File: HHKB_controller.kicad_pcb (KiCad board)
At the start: 2 copper layers, 141.5 x 36 mm, 82 parts, among them CN1 CONN_15, CN2 CONN_13, J1 USB_MINI_MICRO_B, P15 ICSP, P16 CONN_2, P21 CONN_1, P22 CONN_1, P23 CONN_1, P24 CONN_1, P25 CONN_1, P26 CONN_1, P27 CONN_1, P28 CONN_1, P29 CONN_1, Q1 MOSFET_N, Q2 MOSFET_N, SW1 SW_PUSH, SW2 SPST, U1 ATMEGA32U4, U2 TAR5SB33, U3 HT7750A, U4 LTC4054, X1 16MHz

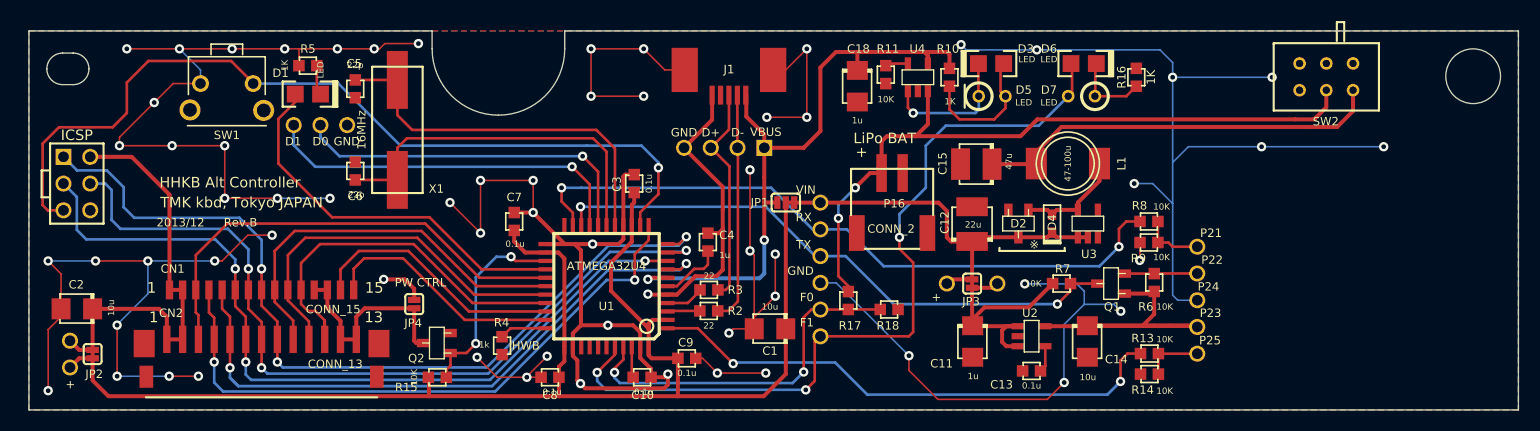
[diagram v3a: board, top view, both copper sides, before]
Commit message: Design initial Rev.B PCB
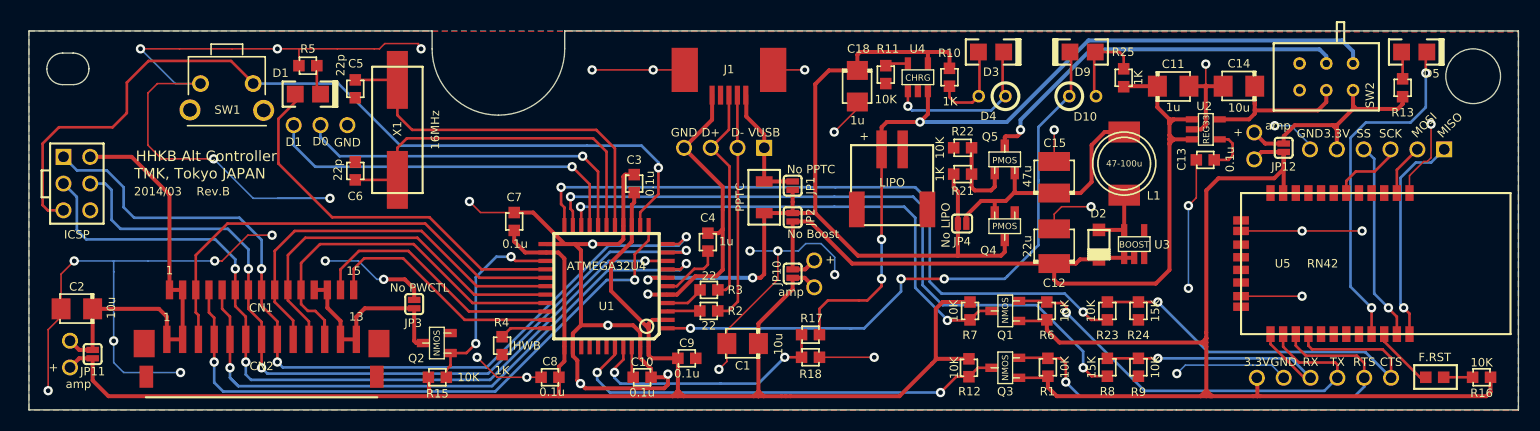
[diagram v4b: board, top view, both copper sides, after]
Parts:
- removed D6: LED, LED_2012_HSOL
- removed D7: LED, LED_TH
- removed F0, F1, P21, P22, P23, P24, P25, P26, P27, P28, P29, RX, TX, VIN: CONN_1, PIN_1
- removed the GND at (152.1, 104.7)
- removed the GND at (100.3, 87.7)
- removed P15: ICSP, AVR_ICSP_3x2
- removed P16: CONN_2, JST_PH2_SMT
- removed R14: 10K, R_1608
- removed VBUS: CONN_1, PIN_1_SQUARE
- added D10: LED, LED_TH, F.Cu at (177.0, 87.0)
- added D9: LED, LED_2012_HSOL, F.Cu at (177.0, 82.8)
- added GND: CONN_1, PIN_1, F.Cu at (107.2, 89.8)
- added JP10: JUMPER, SOLDER_JUMPER_2, F.Cu at (149.4, 103.8)
- added JP11: JUMPER, SOLDER_JUMPER_2, F.Cu at (83.0, 111.5)
- added JP12: JUMPER, SOLDER_JUMPER_2, F.Cu at (196.1, 91.9)
- added P10: CONN_1, PIN_1, F.Cu at (80.8, 110.2)
- added P100: CONN_2, JST_PH2_SMT, F.Cu at (157.9, 92.0)
- added P11: CONN_1, PIN_1, F.Cu at (151.5, 102.6)
- added P110: CONN_1, PIN_1, F.Cu at (193.6, 113.8)
- added P111: CONN_1, PIN_1, F.Cu at (198.7, 113.8)
- added P112: CONN_1, PIN_1, F.Cu at (201.2, 113.8)
- added P113: CONN_1, PIN_1, F.Cu at (196.1, 113.8)
- added P114: CONN_1, PIN_1, F.Cu at (206.3, 113.8)
- added P115: CONN_1, PIN_1, F.Cu at (203.8, 113.8)
- added P12: CONN_1, PIN_1, F.Cu at (151.5, 105.2)
- added P120: CONN_1, PIN_1_SQUARE, F.Cu at (211.3, 92.0)
- added P121: CONN_1, PIN_1, F.Cu at (208.8, 92.0)
- added P122: CONN_1, PIN_1, F.Cu at (206.2, 92.0)
- added P123: CONN_1, PIN_1, F.Cu at (203.7, 92.0)
- added P124: CONN_1, PIN_1, F.Cu at (201.2, 92.0)
- added P125: CONN_1, PIN_1, F.Cu at (198.6, 92.0)
- added P130: CONN_1, PIN_1, F.Cu at (193.3, 90.5)
- added P131: CONN_1, PIN_1, F.Cu at (193.3, 93.0)
- added P8: CONN_3X2, AVR_ICSP_3x2, F.Cu at (81.5, 95.3)
- added P9: CONN_1, PIN_1, F.Cu at (80.8, 112.8)
- added PPTC1: PPTC, PPTC_nano, F.Cu at (146.8, 96.6)
- added Q3: NMOS, MOS_FET_SOT23-3_HSOL, F.Cu at (169.7, 112.8)
- added Q4: PMOS, MOS_FET_SOT23-3_HSOL, F.Cu at (169.6, 99.3)
- added Q5: PMOS, MOS_FET_SOT23-3_HSOL, F.Cu at (169.6, 93.0)
- added R1: 10K, R_1608, F.Cu at (173.7, 112.8)
- added R12: 10K, R_1608, F.Cu at (166.2, 112.8)
- added R19: 0, R_1608_NOGUIDE, F.Cu at (210.4, 113.7)
- added R21: 1K, R_1608, F.Cu at (165.6, 94.4)
- added R22: 10K, R_1608, F.Cu at (165.6, 91.9)
- added R23: 10K, R_1608, F.Cu at (179.3, 107.4)
- added R24: 15K, R_1608, F.Cu at (182.3, 107.4)
- added R25: 1K, R_1608, F.Cu at (180.9, 85.2)
- added U5: RN42, RN42, F.Cu at (208.1, 96.2)
- added VUSB: CONN_1, PIN_1_SQUARE, F.Cu at (146.8, 91.9)
- D2: value MA721 -> Schottky; footprint SOT23-3_HSOL -> D_SOD123
- D4: value RB521 -> LED; footprint D_SC79 -> LED_TH
- D5: footprint LED_TH -> LED_2012_HSOL
- JP1: value JUMPER3 -> JUMPER; footprint SOLDER_JUMPER_3 -> SOLDER_JUMPER_2
- Q1, Q2: value MOSFET_N -> NMOS
- R13: value 10K -> 470
- R16: value 1K -> 10K
- R4: value 1k -> 1K
- R9: value 10K -> 15K
- SW2: value SPST -> SW_DPDT
- U2: value TAR5SB33 -> REG33
- U3: value HT7750A -> BOOST
- U4: value LTC4054 -> CHRG
- moved JP2 67.8 mm to (149.4, 98.5), turned to 270 degrees
- moved JP3 53.0 mm to (113.5, 106.8), turned to 270 degrees
- moved JP4 52.6 mm to (165.6, 99.1), turned to 0 degrees
- moved R16 43.5 mm to (214.9, 113.7), turned to 180 degrees
- moved D5 40.3 mm to (208.5, 82.8), turned to 0 degrees
- moved R13 34.9 mm to (207.4, 86.2), turned to 90 degrees
- moved C11 30.8 mm to (185.6, 86.0), turned to 0 degrees
- moved C14 28.2 mm to (191.8, 86.0), turned to 180 degrees
- moved C13 26.0 mm to (188.7, 93.0)
- moved U2 25.7 mm to (188.7, 90.2)
- moved R8 14.4 mm to (179.3, 112.8), turned to 90 degrees
- moved D4 13.4 mm to (168.4, 87.0), turned to 0 degrees
- moved R9 11.9 mm to (182.3, 112.8), turned to 270 degrees
- moved R6 10.6 mm to (173.6, 107.4)
- moved Q1 10.4 mm to (169.7, 107.4)
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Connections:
- net BT_LIPO renamed LIPO_SENSE
- C1 pad 1: VIN -> 5V_BOOST
- C11 pad 1: VIN -> 5V_BOOST
- C12 pad 1: VIN -> 5V_BOOST
- C14 pad 1: +3.3V -> /bluetooth/3.3V_OUT
- C15 pad 1: /bluetooth/VBAT -> /bluetooth/PSEL
- C18 pad 1: VBUS -> VUSB
- C2 pad 1: VIN -> 5V_BOOST
- C3 pad 1: VIN -> 5V_BOOST
- C7 pad 1: VIN -> 5V_BOOST
- C8 pad 1: VIN -> 5V_BOOST
- C9 pad 1: VIN -> 5V_BOOST
- CN1 pad 1: VIN -> 5V_BOOST
- CN1 pad 2: VIN -> 5V_BOOST
- CN2 pad 1: VIN -> 5V_BOOST
- CN2 pad 2: VIN -> 5V_BOOST
- D2 pad 1: N-0000051 -> N-0000064
- D2 pad 2: N-0000075 -> 5V_BOOST
- D3 pad 1: N-0000069 -> N-0000067
- D3 pad 2: N-0000046 -> N-0000049
- D4 pad 1: N-0000051 -> N-0000067
- D4 pad 2: VIN -> N-0000049
- D5 pad 1: N-0000069 -> N-0000046
- D5 pad 2: N-0000046 -> /bluetooth/LED_STS
- J1 pad 1: VBUS -> /VUSB_RAW
- JP1 pad 1: VBUS -> /VUSB_RAW
- JP1 pad 2: VIN -> VUSB
- JP2 pad 1: VIN -> VUSB
- JP2 pad 2: VIN -> 5V_BOOST
- JP3 pad 1: VIN -> GND
- JP3 pad 2: VIN -> /HHKB_GND
- JP4 pad 1: GND -> VUSB
- JP4 pad 2: /HHKB_GND -> /bluetooth/PSEL
- L1 pad 1: N-0000051 -> N-0000064
- L1 pad 2: /bluetooth/VBAT -> /bluetooth/PSEL
- R10 pad 1: N-0000069 -> N-0000067
- R10 pad 2: VBUS -> VUSB
- R13 pad 1: BT_DTR -> +3.3V
- R13 pad 2: /bluetooth/DTR_33 -> N-0000046
- R15 pad 1: VIN -> 5V_BOOST
- R16 pad 1: N-0000045 -> +3.3V
- R16 pad 2: GND -> N-0000043
- R17 pad 1: N-0000047 -> /bluetooth/LIPO_RAW
- R7 pad 1: VIN -> 5V_BOOST
- SW2 pad 1: N-0000047 -> /bluetooth/LIPO_SW
- SW2 pad 2: /bluetooth/VBAT -> /bluetooth/LIPO_RAW
- SW2 pad 3: (no net) -> N-0000059
- SW2 pad 4: (no net) -> /bluetooth/3.3V_OUT
- SW2 pad 5: (no net) -> +3.3V
- SW2 pad 6: (no net) -> N-0000060
- U1 pad 1: BT_DTR -> BT_INDICATOR
- U1 pad 14: VIN -> 5V_BOOST
- U1 pad 2: VIN -> 5V_BOOST
- U1 pad 22: /PD5 -> BT_CTS
- U1 pad 24: VIN -> 5V_BOOST
- U1 pad 34: VIN -> 5V_BOOST
- U1 pad 40: BT_INDICATOR -> BT_RTS
- U1 pad 44: VIN -> 5V_BOOST
- U1 pad 7: VBUS -> VUSB
- U2 pad 1: VIN -> 5V_BOOST
- U2 pad 3: VIN -> 5V_BOOST
- U2 pad 5: +3.3V -> /bluetooth/3.3V_OUT
- U3 pad 1: VIN -> 5V_BOOST
- U3 pad 2: VIN -> 5V_BOOST
- U3 pad 5: N-0000051 -> N-0000064
- U4 pad 1: N-0000046 -> N-0000049
- U4 pad 3: N-0000047 -> /bluetooth/LIPO_RAW
- U4 pad 4: VBUS -> VUSB
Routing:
- net 5V_BOOST: track 0.00 -> 288.8 mm
- net VIN: track 243.0 -> 0.00 mm
- net +3.3V: track 31.4 -> 130.6 mm
- net GND: track 438.5 -> 346.1 mm, vias 64 -> 41
- net VUSB: track 0.00 -> 84.6 mm, vias 0 -> 2
- net /bluetooth/LIPO_RAW: track 0.00 -> 77.4 mm, vias 0 -> 3
- net N-0000047: track 67.0 -> 0.00 mm, vias 2 -> 0
- net BT_CTS: track 0.00 -> 65.4 mm, vias 0 -> 2
- net VBUS: track 61.4 -> 0.00 mm, vias 2 -> 0
- net BT_DTR: track 50.5 -> 0.00 mm, vias 2 -> 0
- net /bluetooth/RTS_33: track 0.00 -> 46.2 mm, vias 0 -> 1
- net BT_RTS: track 0.00 -> 42.8 mm, vias 0 -> 2
- net /bluetooth/CTS_33: track 0.00 -> 41.3 mm, vias 0 -> 1
- net /bluetooth/VBAT: track 39.0 -> 0.00 mm
- net /bluetooth/LIPO_SW: track 0.00 -> 36.5 mm, vias 0 -> 1
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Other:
- board text added: "2014/03"
- board text added: "3.3V"
- board text added: "CTS"
- board text added: "F.RST"
- board text added: "GND"
- board text added: "LIPO"
- board text added: "MISO"
- board text added: "MOSI"
- board text added: "No Boost"
- board text added: "No LIPO"
- board text added: "No PPTC"
- board text added: "No PWCTL"
- board text added: "RTS"
- board text added: "RX"
- board text added: "SCK"
- board text added: "SS"
- board text added: "TMK, Tokyo JAPAN"
- board text added: "TX"
- board text added: "amp"
- board text removed: "2013/12"
- board text removed: "LiPo BAT"
- board text removed: "PW CTRL"
- board text removed: "TMK kbd, Tokyo JAPAN"
- board text removed: "※"

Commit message: Clean files
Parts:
- moved D5 22.8 mm to (185.7, 82.8), turned to 180 degrees
- moved R13 17.2 mm to (190.6, 82.8), turned to 180 degrees
- moved R25 0.40 mm to (180.7, 85.6)
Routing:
- net GND: track 346.1 -> 448.7 mm, vias 41 -> 50
- net +3.3V: track 130.6 -> 147.6 mm
- net N-0000049: track 15.8 -> 22.2 mm
- net /bluetooth/LED_STS: track 33.1 -> 37.5 mm
- net /bluetooth/LIPO_RAW: track 77.4 -> 80.3 mm
- net /PB4: track 37.9 -> 36.6 mm
- net BT_CTS: track 65.4 -> 66.2 mm
- net /PB5: track 36.3 -> 35.5 mm
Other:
- board text added: "HHKB Alt Controller TMK, Tokyo JAPAN"
- board text added: "LiPo"
- board text added: "No LiPo"
- board text removed: "HHKB Alt Controller"
- board text removed: "LIPO"
- board text removed: "No LIPO"
- board text removed: "TMK, Tokyo JAPAN"

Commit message: Change module for Schottky diode D2
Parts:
- D2: footprint D_SOD123 -> keyboard_parts:D_SOD123
- moved D2 0.23 mm to (178.3, 101.0)

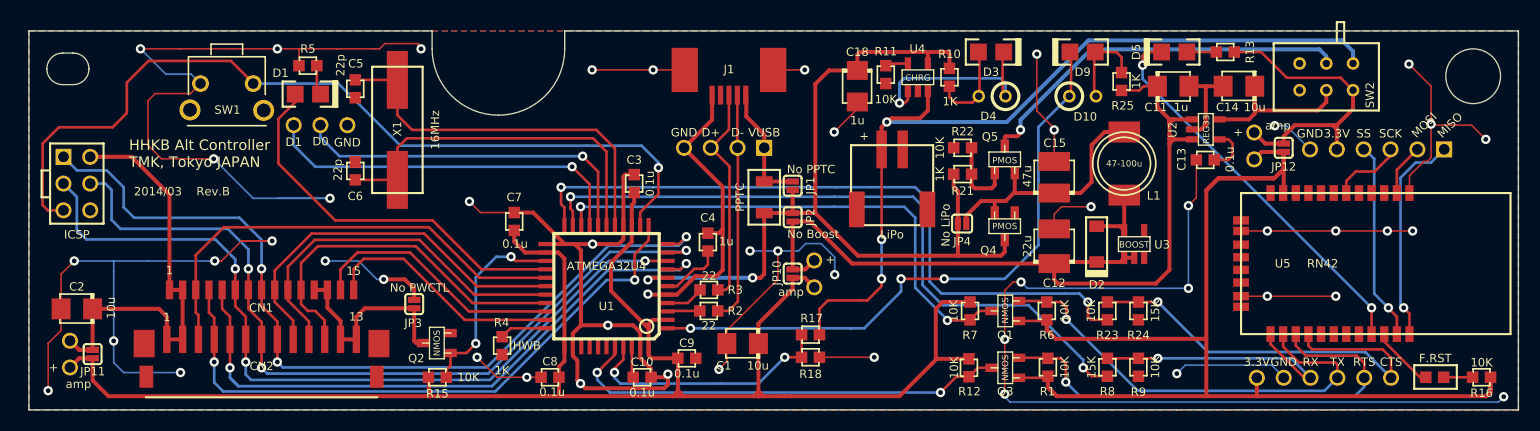
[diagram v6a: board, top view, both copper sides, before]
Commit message: Fix many fixes of rev.B errata
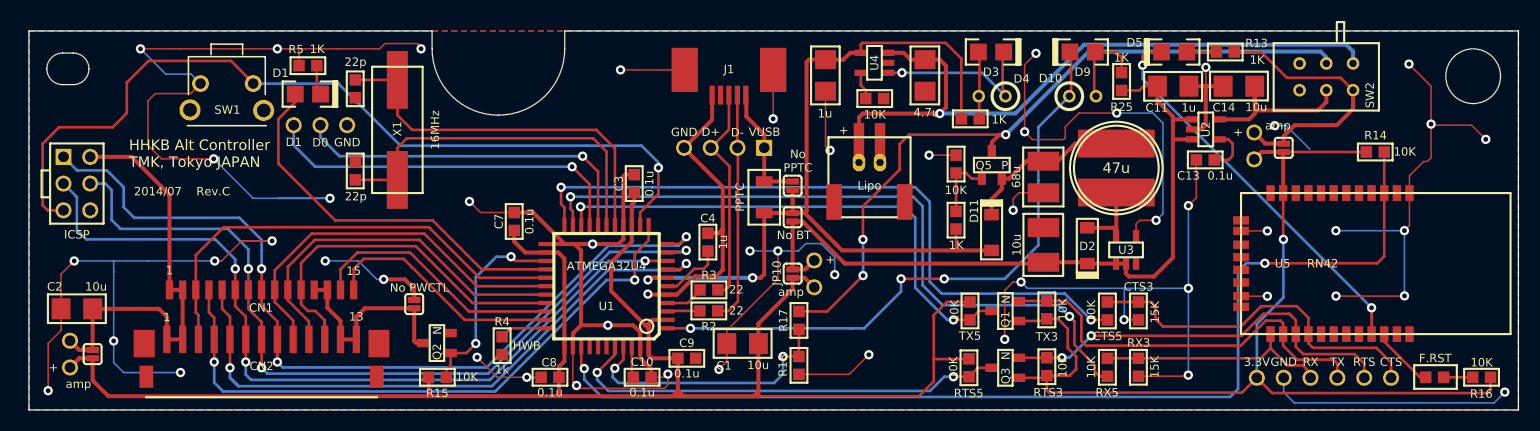
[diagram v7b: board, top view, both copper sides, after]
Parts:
- removed D0, P121, P122, P123, P124, P125: CONN_1, PIN_1
- removed JP4: JUMPER, SOLDER_JUMPER_2
- removed P120: CONN_1, PIN_1_SQUARE
- removed Q4: PMOS, MOS_FET_SOT23-3_HSOL
- added C16: 4.7u, keyboard_parts:C_3216, F.Cu at (162.0, 85.0)
- added D11: Schottky diode, keyboard_parts:D_SOD123, F.Cu at (168.3, 100.0)
- added P6: D0, keyboard_parts:PIN_1, F.Cu at (104.6, 89.8)
- added R14: 10K, keyboard_parts:R_1608, F.Cu at (204.8, 92.3)
- C1, C11, C14, C18, C2: footprint C_3216 -> keyboard_parts:C_3216
- C10, C13, C3, C4, C5, C6, C7, C8, C9: footprint C_1608 -> keyboard_parts:C_1608
- C12: value 22u -> 10u; footprint C_3228 -> keyboard_parts:C_3228
- C15: value 47u -> 68u; footprint C_3225 -> keyboard_parts:C_3225
- D2: value Schottky -> Schottky diode
- J1: value USB_MINI_MICRO_B -> USB_mini_micro_B
- L1: value 47-100u -> 47u; footprint L_6x6MM -> keyboard_parts:L_7x7MM
- P1, P7: renamed from GND; value CONN_1 -> GND
- P100: value CONN_2 -> Lipo; footprint JST_PH2_SMT -> keyboard_parts:JST_PH2_SMT_TH
- P2: renamed from D+; value CONN_1 -> D+
- P3: renamed from D-; value CONN_1 -> D-
- P4: renamed from VUSB; value CONN_1 -> VUSB
- P5: renamed from D1; value CONN_1 -> D1
- Q1, Q2, Q3: value NMOS -> N; footprint MOS_FET_SOT23-3_HSOL -> keyboard_parts:MOS_FET_SOT23-3_HSOL
- Q5: value PMOS -> P; footprint MOS_FET_SOT23-3_HSOL -> keyboard_parts:MOS_FET_SOT23-3_HSOL
- R1, R10, R11, R12, R15, R16, R17, R18, R2, R21, R22, R23, R24, R25, R3, R5, R6, R7, R8, R9: footprint R_1608 -> keyboard_parts:R_1608
- R13: value 470 -> 1K; footprint R_1608 -> keyboard_parts:R_1608
- R4: value 1K -> 1k; footprint R_1608 -> keyboard_parts:R_1608
- U2: value REG33 -> TAR5SB33; footprint SOT23-5_HSOL -> keyboard_parts:SOT23-5_HSOL
- U3: value BOOST -> NCP1402; footprint SOT23-5_HSOL -> keyboard_parts:SOT23-5_HSOL
- U4: value CHRG -> MCP73831; footprint SOT23-5_HSOL -> keyboard_parts:SOT23-5_HSOL
- moved R21 4.42 mm to (165.0, 98.8), turned to 90 degrees
- moved R10 4.42 mm to (166.3, 89.2), turned to 180 degrees
- moved U4 4.35 mm to (157.2, 83.8), turned to 90 degrees
- moved C18 3.19 mm to (152.6, 85.0)
- moved R11 2.51 mm to (157.2, 87.2), turned to 0 degrees
- moved P100 2.28 mm to (155.8, 91.3)
- moved R17 1.74 mm to (150.1, 108.3), turned to 270 degrees
- moved R22 1.67 mm to (165.0, 93.5), turned to 90 degrees
- moved R18 1.34 mm to (150.1, 112.6), turned to 270 degrees
- moved Q5 1.33 mm to (168.4, 93.5)
- moved C12 1.03 mm to (173.3, 101.1)
- moved C15 1.03 mm to (173.3, 94.7), turned to 270 degrees
- moved U3 0.95 mm to (181.1, 101.6)
- moved D2 0.89 mm to (177.4, 101.2)
- moved L1 0.86 mm to (180.2, 93.8)
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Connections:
- R17 pad 1: /bluetooth/LIPO_RAW -> /bluetooth/LIPO_SW
- U1 pad 36: /PF7 -> BT_CONN
- U5 pad 3: N-0000069 -> BT_CONN
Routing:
- net BT_CONN: track 0.00 -> 101.9 mm, vias 0 -> 2
- net /bluetooth/LIPO_SW: track 36.5 -> 68.9 mm, vias 1 -> 3
- net +3.3V: track 147.6 -> 121.0 mm, vias 0 -> 1
- net /bluetooth/SPI_MISO: track 20.5 -> 0.00 mm, vias 1 -> 0
- net /bluetooth/SPI_SS: track 18.9 -> 0.00 mm, vias 1 -> 0
- net /bluetooth/LIPO_RAW: track 80.3 -> 66.3 mm, vias 3 -> 1
- net 5V_BOOST: track 289.2 -> 277.8 mm
- net GND: track 448.7 -> 457.7 mm, vias 50 -> 52
- net /bluetooth/PSEL: track 24.1 -> 16.1 mm
- net /bluetooth/SPI_SCK: track 6.94 -> 0.00 mm
- net /bluetooth/RTS_33: track 46.2 -> 39.3 mm, vias 1 -> 2
- net /bluetooth/CTS_33: track 41.3 -> 34.5 mm, vias 1 -> 0
- net Net-(D3-Pad2): track 22.2 -> 16.4 mm
- net /bluetooth/SPI_MOSI: track 4.96 -> 0.00 mm
- net /bluetooth/TX_33: track 43.3 -> 38.7 mm, vias 1 -> 0
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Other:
- board text added: "2014/07"
- board text added: "CTS3"
- board text added: "CTS5"
- board text added: "No BT"
- board text added: "RTS3"
- board text added: "RTS5"
- board text added: "RX3"
- board text added: "RX5"
- board text added: "Rev.C"
- board text added: "TX3"
- board text added: "TX5"
- board text removed: "2014/03"
- board text removed: "LiPo"
- board text removed: "MISO"
- board text removed: "MOSI"
- board text removed: "No Boost"
- board text removed: "No LiPo"
- board text removed: "Rev.B"
- board text removed: "SCK"
- board text removed: "SS"

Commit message: Change for rev.C
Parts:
- added R20: 15K, keyboard_parts:R_1608, F.Cu at (204.8, 91.5)
- C18: value 1u -> 4.7u
- P100: value Lipo -> CONN_2
- P5: value D1 -> PD1
- P6: value D0 -> PD0
- R13: value 1K -> 470
- R19: value 0 -> F.RST
- U1: footprint TQFP44 -> keyboard_parts:QFP44
- moved D5 21.5 mm to (207.2, 83.9), turned to 270 degrees
- moved R13 20.1 mm to (209.2, 90.4), turned to 90 degrees
- moved C6 15.6 mm to (123.2, 97.0), turned to 180 degrees
- moved C5 13.1 mm to (115.4, 97.0), turned to 0 degrees
- moved X1 7.88 mm to (119.3, 92.8), turned to 0 degrees
- moved R14 4.80 mm to (200.1, 91.5)
- moved C7 1.84 mm to (121.9, 100.4), turned to 180 degrees
- moved C13 0.60 mm to (188.7, 93.7)
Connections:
- D3 pad 2: Net-(D3-Pad2) -> ~CHRG
- D4 pad 2: Net-(D3-Pad2) -> ~CHRG
- J1 pad 4: Net-(J1-Pad4) -> (no net)
- R14 pad 1: +3.3V -> BT_CONN
- R14 pad 2: BT_CONN -> /bluetooth/CONN
- R17 pad 1: /bluetooth/LIPO_SW -> /bluetooth/LIPO_RAW
- SW2 pad 3: Net-(SW2-Pad3) -> (no net)
- SW2 pad 6: Net-(SW2-Pad6) -> (no net)
- U1 pad 37: /PF6 -> LINKED
- U1 pad 38: /PF5 -> ~CHRG
- U1 pad 39: /PF4 -> (no net)
- U3 pad 3: Net-(U3-Pad3) -> (no net)
- U4 pad 1: Net-(D3-Pad2) -> ~CHRG
- U5 pad 10: Net-(U5-Pad10) -> (no net)
- U5 pad 17: Net-(U5-Pad17) -> (no net)
- U5 pad 18: Net-(U5-Pad18) -> (no net)
- U5 pad 19: Net-(U5-Pad19) -> LINKED
- U5 pad 2: /bluetooth/SPI_MOSI -> (no net)
- U5 pad 20: Net-(U5-Pad20) -> (no net)
- U5 pad 23: /bluetooth/SPI_SS -> (no net)
- U5 pad 24: /bluetooth/SPI_MISO -> (no net)
- U5 pad 3: BT_CONN -> /bluetooth/CONN
- U5 pad 30: Net-(U5-Pad30) -> (no net)
- U5 pad 31: /bluetooth/LED_ACT -> (no net)
- U5 pad 32: Net-(U5-Pad32) -> (no net)
- U5 pad 33: Net-(U5-Pad33) -> (no net)
- U5 pad 34: Net-(U5-Pad34) -> (no net)
- U5 pad 35: Net-(U5-Pad35) -> (no net)
- U5 pad 4: Net-(U5-Pad4) -> (no net)
- U5 pad 5: /bluetooth/RN42_RST -> (no net)
- U5 pad 6: /bluetooth/SPI_SCK -> (no net)
- U5 pad 7: Net-(U5-Pad7) -> (no net)
- U5 pad 8: Net-(U5-Pad8) -> (no net)
- U5 pad 9: Net-(U5-Pad9) -> (no net)
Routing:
- net LINKED: track 0.00 -> 83.1 mm, vias 0 -> 2
- net ~CHRG: track 0.00 -> 69.6 mm, vias 0 -> 4
- net /bluetooth/LIPO_SW: track 68.9 -> 35.8 mm, vias 3 -> 1
- net /bluetooth/LIPO_RAW: track 66.3 -> 85.9 mm, vias 1 -> 3
- net GND: track 457.7 -> 438.3 mm, vias 52 -> 57
- net Net-(C6-Pad1): track 34.9 -> 17.8 mm
- net Net-(D3-Pad2): track 16.4 -> 0.00 mm, vias 1 -> 0
- net /bluetooth/LED_STS: track 37.5 -> 25.8 mm
- net /bluetooth/CONN: track 0.00 -> 8.44 mm
- net /PD0: track 34.0 -> 40.4 mm
- net Net-(C5-Pad1): track 36.7 -> 30.6 mm
- net Net-(D5-Pad1): track 2.90 -> 8.80 mm
- net +3.3V: track 121.0 -> 115.2 mm
- net /PD1: track 35.5 -> 41.2 mm
- net (no net): track 4.28 -> 0.00 mm, vias 1 -> 0
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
